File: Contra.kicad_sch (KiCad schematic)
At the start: 102 parts, among them J1 Conn_01x04, J2 Conn_01x02, SW1 SW_PUSH, SW2 SW_SPDT, U1 ProMicro

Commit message: add in NC symbols
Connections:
- no-connect marks 0 -> 6
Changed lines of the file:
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@@
 		(color 0 0 0 0)
 	)
+	(no_connect
+		(at 120.65 161.29)
+	)
+	(no_connect
+		(at 95.25 187.96)
+	)
+	(no_connect
+		(at 80.01 153.67)
+	)
+	(no_connect
+		(at 97.79 187.96)
+	)
+	(no_connect
+		(at 100.33 187.96)
+	)
+	(no_connect
+		(at 80.01 156.21)
+	)
 	(wire
 		(pts
@@
 	(wire
 		(pts
+			(xy 80.01 153.67) (xy 81.28 153.67)
+		)
+		(stroke
+			(width 0)
+			(type default)
+		)
+	)
+	(wire
+		(pts
 			(xy 176.53 96.52) (xy 195.58 96.52)
 		)
@@
 	(wire
 		(pts
+			(xy 119.38 161.29) (xy 120.65 161.29)
+		)
+		(stroke
+			(width 0)
+			(type default)
+		)
+	)
+	(wire
+		(pts
 			(xy 138.43 77.47) (xy 157.48 77.47)
 		)
@@
 	(wire
 		(pts
+			(xy 100.33 186.69) (xy 100.33 187.96)
+		)
+		(stroke
+			(width 0)
+			(type default)
+		)
+	)
+	(wire
+		(pts
 			(xy 81.28 115.57) (xy 100.33 115.57)
 		)
@@
 	(wire
 		(pts
+			(xy 80.01 156.21) (xy 81.28 156.21)
+		)
+		(stroke
+			(width 0)
+			(type default)
+		)
+	)
+	(wire
+		(pts
 			(xy 214.63 106.68) (xy 214.63 110.49)
 		)
@@
 	(wire
 		(pts
+			(xy 97.79 186.69) (xy 97.79 187.96)
+		)
+		(stroke
+			(width 0)
+			(type default)
+		)
+	)
+	(wire
+		(pts
 			(xy 195.58 87.63) (xy 195.58 91.44)
 		)
@@
 		)
 		(stroke
+			(width 0)
+			(type default)
+		)
+	)
+	(wire
+		(pts
+			(xy 95.25 186.69) (xy 95.25 187.96)
+		)
+		(stroke

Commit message: connect rows and colls
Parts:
- J1: footprint Connector_PinHeader_2.54mm:PinHeader_1x04_P2.54mm_Vertical -> Connector_PinHeader_2.54mm:PinHeader_1x04_P2.54mm_Horizontal
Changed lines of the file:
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@@
 			)
 		)
-		(property "Footprint" "Connector_PinHeader_2.54mm:PinHeader_1x04_P2.54mm_Vertical"
+		(property "Footprint" "Connector_PinHeader_2.54mm:PinHeader_1x04_P2.54mm_Horizontal"
 			(at 45.72 152.4 0)
 			(hide yes)

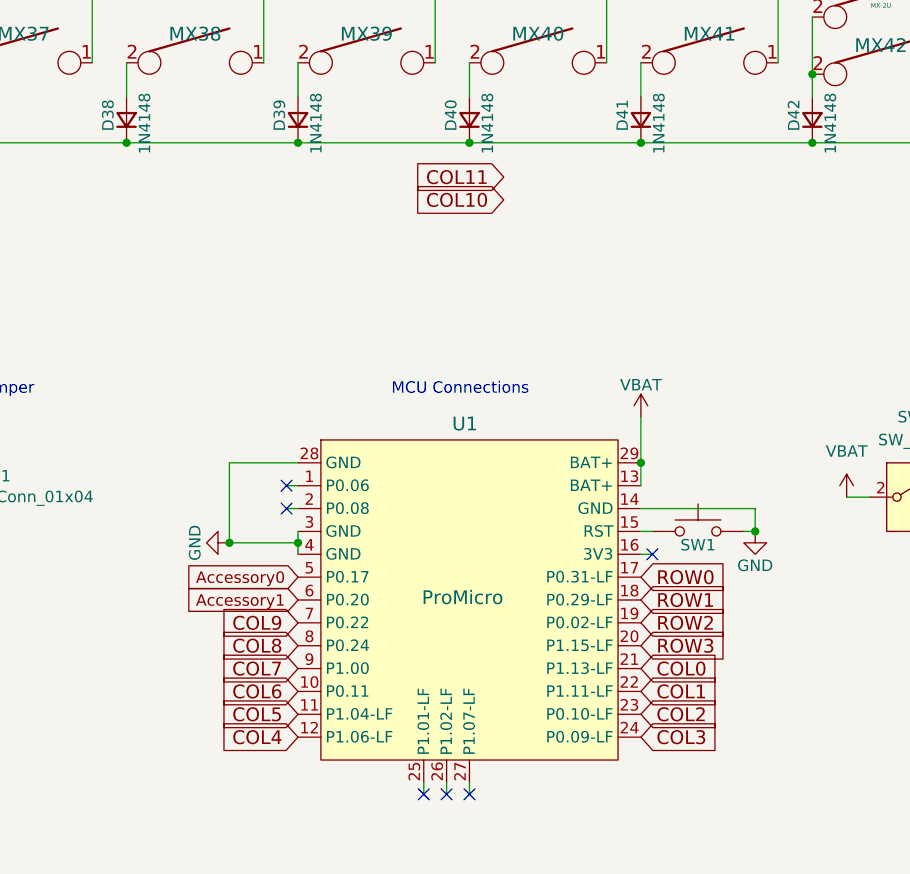
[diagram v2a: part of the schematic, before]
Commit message: update pinout of nice!nano
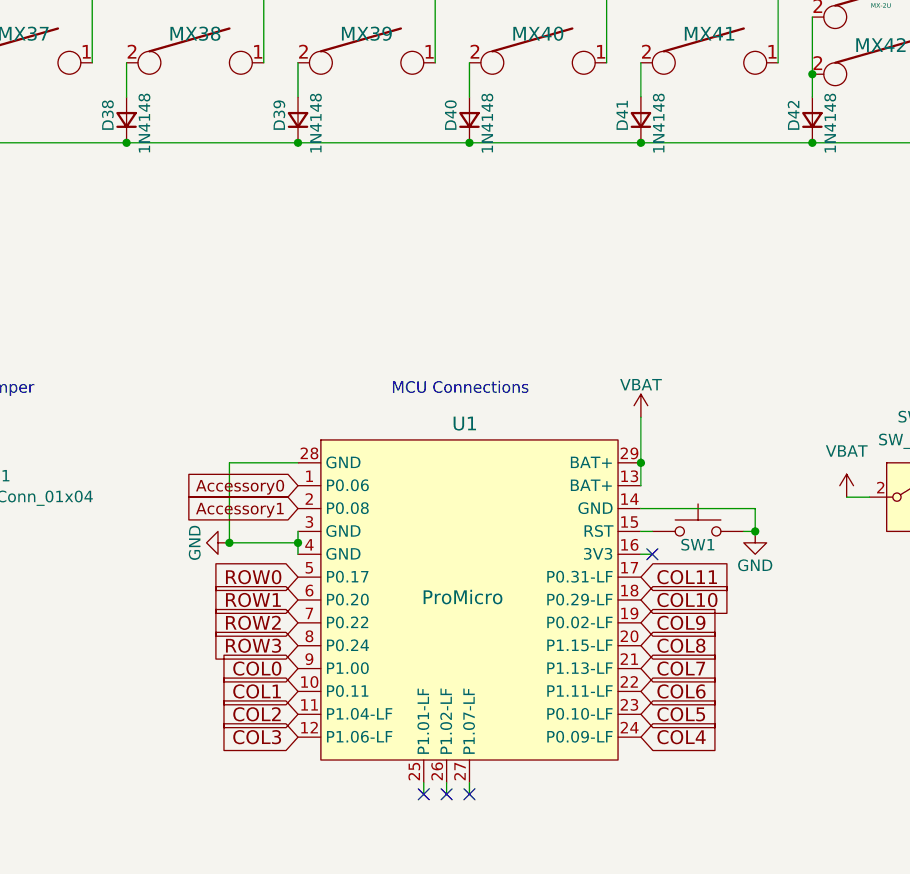
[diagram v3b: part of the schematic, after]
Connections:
- net Accessory0: now also U1.1 (P0.06); no longer U1.5 (P0.17)
- net Accessory1: now also U1.2 (P0.08); no longer U1.6 (P0.20)
- net COL0: now also U1.9 (P1.00); no longer U1.21 (P1.13-LF)
- net COL1: now also U1.10 (P0.11); no longer U1.22 (P1.11-LF)
- net COL10: now also U1.18 (P0.29-LF)
- net COL11: now also U1.17 (P0.31-LF)
- net COL2: now also U1.11 (P1.04-LF); no longer U1.23 (P0.10-LF)
- net COL3: now also U1.12 (P1.06-LF); no longer U1.24 (P0.09-LF)
- net COL4: now also U1.24 (P0.09-LF); no longer U1.12 (P1.06-LF)
- net COL5: now also U1.23 (P0.10-LF); no longer U1.11 (P1.04-LF)
- net COL6: now also U1.22 (P1.11-LF); no longer U1.10 (P0.11)
- net COL7: now also U1.21 (P1.13-LF); no longer U1.9 (P1.00)
- net COL8: now also U1.20 (P1.15-LF); no longer U1.8 (P0.24)
- net COL9: now also U1.19 (P0.02-LF); no longer U1.7 (P0.22)
- net ROW0: now also U1.5 (P0.17); no longer U1.17 (P0.31-LF)
- net ROW1: now also U1.6 (P0.20); no longer U1.18 (P0.29-LF)
- net ROW2: now also U1.7 (P0.22); no longer U1.19 (P0.02-LF)
- net ROW3: now also U1.8 (P0.24); no longer U1.20 (P1.15-LF)
- no-connect marks 6 -> 4

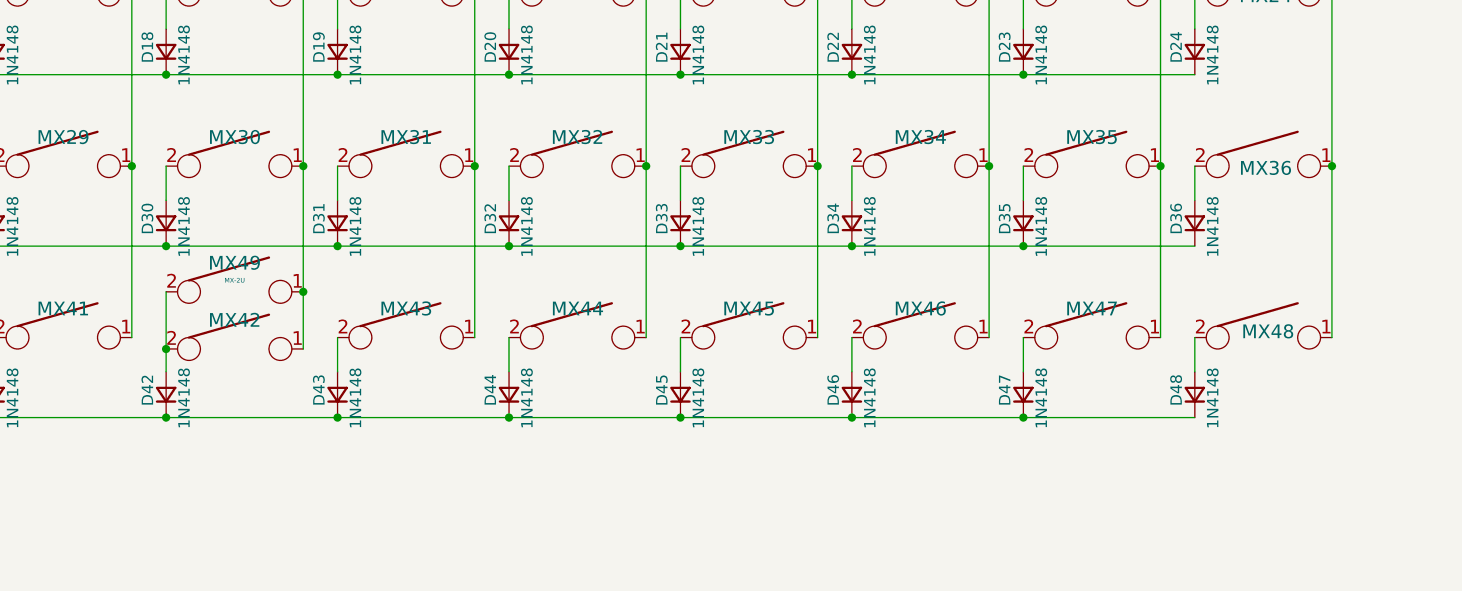
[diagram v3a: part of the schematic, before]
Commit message: remove 2 1U keys for a single 2U key for space
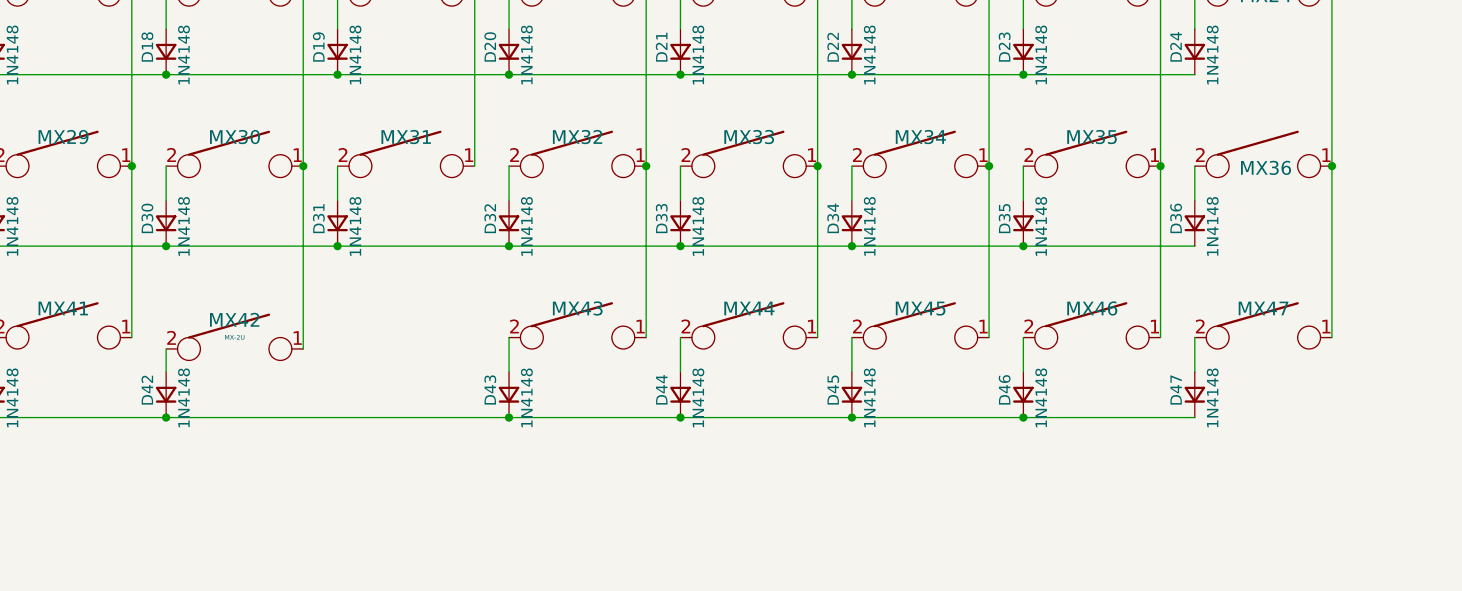
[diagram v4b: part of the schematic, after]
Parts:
- removed D48: 1N4148, Diode_THT:D_DO-35_SOD27_P7.62mm_Horizontal, symbol Device:D_Small
- removed MX48: MX-1U, MX_Hotswap:MX-Hotswap-1U, symbol keyboard_parts:KEYSW
- removed MX49: MX-2U, MX_Hotswap:MX-Hotswap-2U-ReversedStabilizers, symbol keyboard_parts:KEYSW
- MX42: value MX-1U -> MX-2U; footprint MX_Hotswap:MX-Hotswap-1U -> MX_Hotswap:MX-Hotswap-2U-ReversedStabilizers
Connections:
- net COL10: now also MX46.1; no longer MX47.1
- net COL11: now also MX47.1
- net COL6: no longer MX43.1
- net COL7: now also MX43.1; no longer MX44.1
- net COL8: now also MX44.1; no longer MX45.1
- net COL9: now also MX45.1; no longer MX46.1
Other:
- moved on the sheet: D43, D44, D45, D46, D47, MX43, MX44, MX45, MX46, MX47

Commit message: make PCB 4 layers
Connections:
- net VBAT: now also SW2.3 (C); no longer SW2.2 (B)
- net at J2.1 (Pin_1): now also SW2.2 (B); no longer SW2.3 (C)
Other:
- moved on the sheet: SW2
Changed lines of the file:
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@@
 	)
 	(junction
-		(at 157.48 160.02)
+		(at 157.48 165.1)
 		(diameter 0)
 		(color 0 0 0 0)
@@
 	(wire
 		(pts
-			(xy 157.48 152.4) (xy 157.48 160.02)
-		)
-		(stroke
-			(width 0)
-			(type default)
-		)
-	)
-	(wire
-		(pts
 			(xy 138.43 58.42) (xy 157.48 58.42)
 		)
@@
 	(wire
 		(pts
-			(xy 134.62 68.58) (xy 134.62 87.63)
+			(xy 144.78 165.1) (xy 157.48 165.1)
 		)
 		(stroke
@@
 	(wire
 		(pts
-			(xy 36.83 58.42) (xy 43.18 58.42)
+			(xy 134.62 68.58) (xy 134.62 87.63)
 		)
 		(stroke
@@
 	(wire
 		(pts
-			(xy 154.94 152.4) (xy 157.48 152.4)
+			(xy 36.83 58.42) (xy 43.18 58.42)
 		)
 		(stroke
@@
 	(wire
 		(pts
+			(xy 157.48 165.1) (xy 157.48 160.02)
+		)
+		(stroke
+			(width 0)
+			(type default)
+		)
+	)
+	(wire
+		(pts
 			(xy 248.92 38.1) (xy 248.92 49.53)
 		)
@@
 	(wire
 		(pts
-			(xy 154.94 157.48) (xy 158.75 157.48)
-		)
-		(stroke
-			(width 0)
-			(type default)
-		)
-	)
-	(wire
-		(pts
 			(xy 210.82 68.58) (xy 210.82 87.63)
 		)
@@
 	(wire
 		(pts
+			(xy 144.78 160.02) (xy 144.78 165.1)
+		)
+		(stroke
+			(width 0)
+			(type default)
+		)
+	)
+	(wire
+		(pts
 			(xy 100.33 77.47) (xy 119.38 77.47)
 		)
@@
 	(wire
 		(pts
+			(xy 154.94 157.48) (xy 158.75 157.48)
+		)
+		(stroke
+			(width 0)
+			(type default)
+		)
+	)
+	(wire
+		(pts
 			(xy 115.57 87.63) (xy 115.57 106.68)
 		)
@@
 	(symbol
 		(lib_id "Switch:SW_SPDT")
-		(at 149.86 154.94 0)
+		(at 149.86 157.48 180)
 		(unit 1)
 		(body_style 1)
@@
 		(fields_autoplaced yes)
 		(property "Reference" "SW2"
-			(at 149.86 146.05 0)
+			(at 149.86 148.59 0)
 			(show_name no)
 			(do_not_autoplace no)
@@
 		)
 		(property "Value" "SW_SPDT"
-			(at 149.86 148.59 0)
+			(at 149.86 151.13 0)
 			(show_name no)
 			(do_not_autoplace no)
@@
 		)
 		(property "Footprint" "Button_Switch_THT:SW_Slide_SPDT_Angled_CK_OS102011MA1Q"
-			(at 149.86 154.94 0)
+			(at 149.86 157.48 0)
 			(hide yes)
 			(show_name no)
@@
 		)
 		(property "Datasheet" ""
-			(at 149.86 162.56 0)
+			(at 149.86 149.86 0)
 			(hide yes)
 			(show_name no)
@@
 		)
 		(property "Description" "Switch, single pole double throw"
-			(at 149.86 154.94 0)
+			(at 149.86 157.48 0)
 			(hide yes)
 			(show_name no)
@@
 	(symbol
 		(lib_id "power:GND")
-		(at 157.48 160.02 0)
+		(at 157.48 165.1 0)
 		(unit 1)
 		(body_style 1)
@@
 		(fields_autoplaced yes)
 		(property "Reference" "#PWR01"
-			(at 157.48 166.37 0)
+			(at 157.48 171.45 0)
 			(hide yes)
 			(show_name no)
@@
 		)
 		(property "Value" "GND"
-			(at 157.48 165.1 0)
+			(at 157.48 170.18 0)
 			(show_name no)
 			(do_not_autoplace no)
@@
 		)
 		(property "Footprint" ""
-			(at 157.48 160.02 0)
+			(at 157.48 165.1 0)
 			(hide yes)
 			(show_name no)
@@
 		)
 		(property "Datasheet" ""
-			(at 157.48 160.02 0)
+			(at 157.48 165.1 0)
 			(hide yes)
 			(show_name no)
@@
 		)
 		(property "Description" "Power symbol creates a global label with name \"GND\" , ground"
-			(at 157.48 160.02 0)
+			(at 157.48 165.1 0)
 			(hide yes)
 			(show_name no)

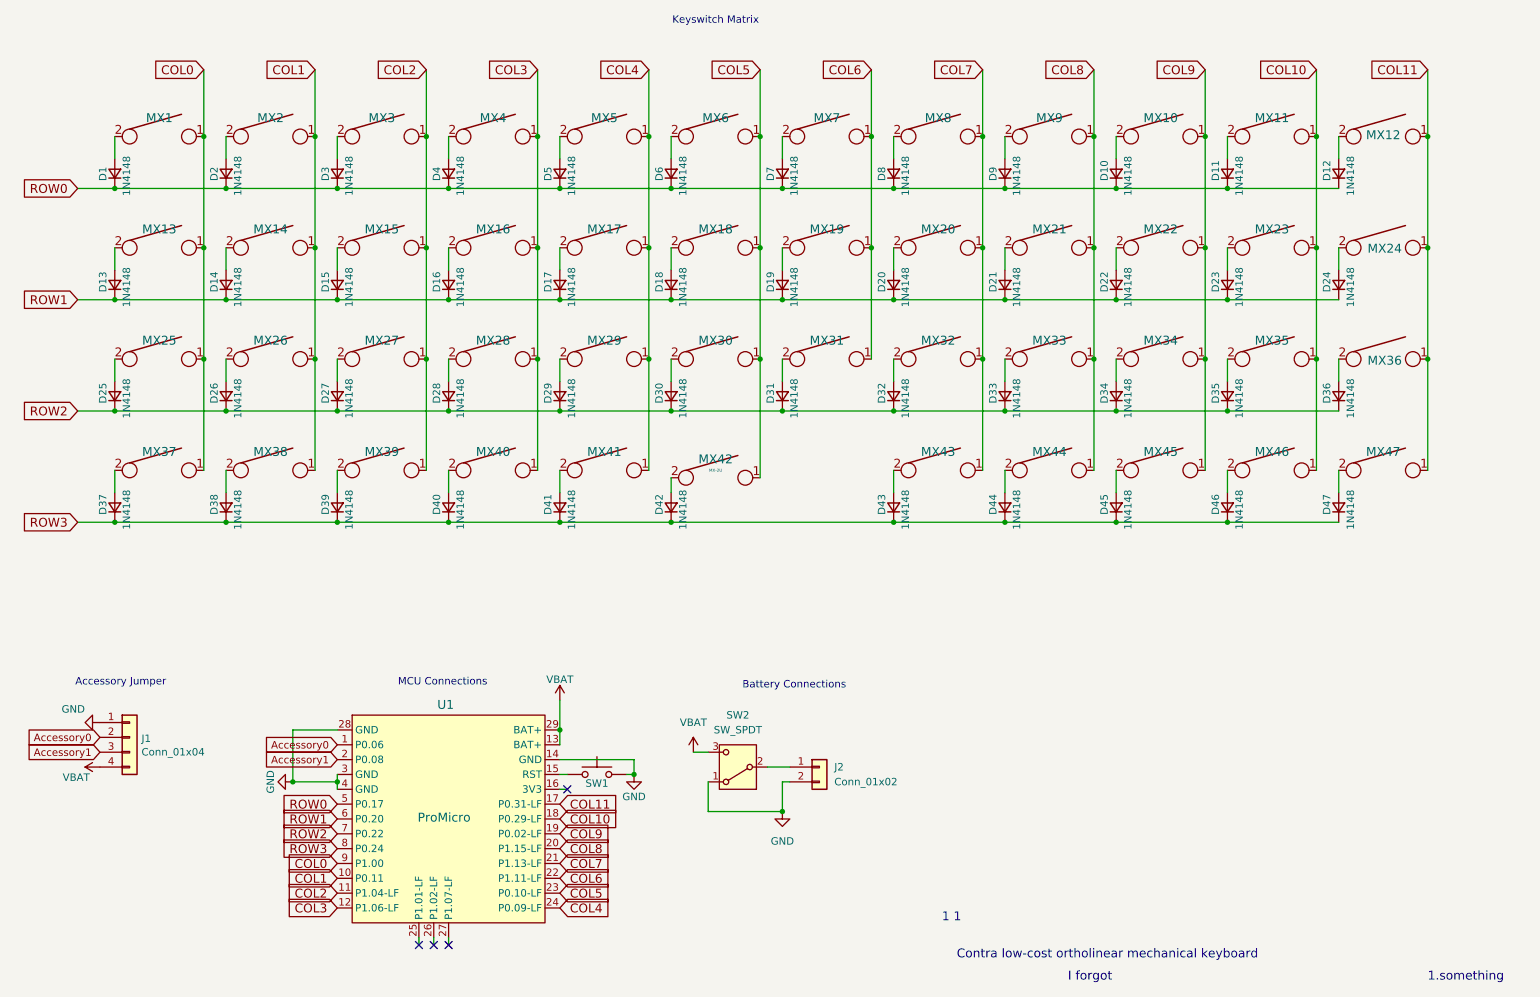
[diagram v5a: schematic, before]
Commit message: start adding in Neopixels
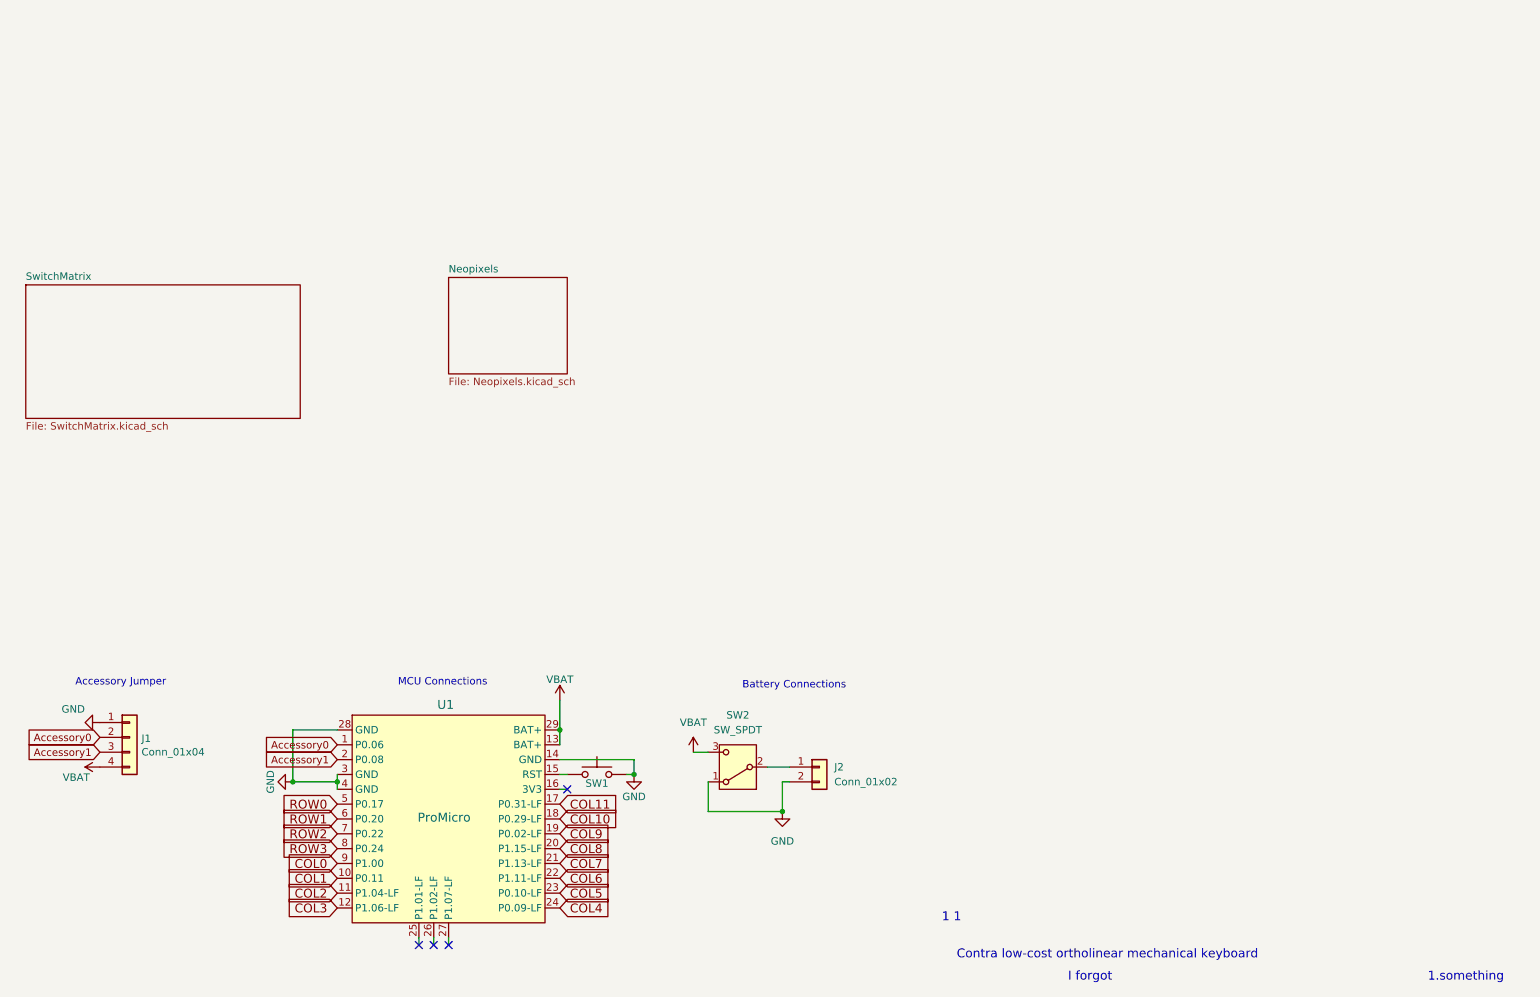
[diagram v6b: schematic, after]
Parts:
- removed D1, D10, D11, D12, D13, D14, D15, D16, D17, D18, D19, D2, D20, D21, D22, D23, D24, D25, D26, D27, D28, D29, D3, D30, D31, D32, D33, D34, D35, D36, D37, D38, D39, D4, D40, D41, D42, D43, D44, D45, D46, D47, D5, D6, D7, D8, D9: 1N4148, Diode_THT:D_DO-35_SOD27_P7.62mm_Horizontal, symbol Device:D_Small
- removed MX1, MX10, MX11, MX12, MX13, MX14, MX15, MX16, MX17, MX18, MX19, MX2, MX20, MX21, MX22, MX23, MX24, MX25, MX26, MX27, MX28, MX29, MX3, MX30, MX31, MX32, MX33, MX34, MX35, MX36, MX37, MX38, MX39, MX4, MX40, MX41, MX43, MX44, MX45, MX46, MX47, MX5, MX6, MX7, MX8, MX9: MX-1U, MX_Hotswap:MX-Hotswap-1U, symbol keyboard_parts:KEYSW
- removed MX42: MX-2U, MX_Hotswap:MX-Hotswap-2U-ReversedStabilizers, symbol keyboard_parts:KEYSW
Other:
- added sheet Neopixels (Neopixels.kicad_sch)
- added sheet SwitchMatrix (SwitchMatrix.kicad_sch)
- note removed: "Keyswitch Matrix"

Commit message: get the Corne reference set up
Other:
- added sheet CorneReference (CorneReference.kicad_sch)
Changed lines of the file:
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@@
+	)
+	(sheet
+		(at 214.63 60.96)
+		(size 53.34 27.94)
+		(exclude_from_sim no)
+		(in_bom yes)
+		(on_board yes)
+		(dnp no)
+		(fields_autoplaced yes)
+		(stroke
+			(width 0.1524)
+			(type solid)
+		)
+		(fill
+			(color 0 0 0 0)
+		)
+		(property "Sheetname" "CorneReference"
+			(at 214.63 60.2484 0)
+			(show_name no)
+			(do_not_autoplace no)
+			(effects
+				(font
+					(size 1.27 1.27)
+				)
+				(justify left bottom)
+			)
+		)
+		(property "Sheetfile" "CorneReference.kicad_sch"
+			(at 214.63 89.4846 0)
+			(show_name no)
+			(do_not_autoplace no)
+			(effects
+				(font
+					(size 1.27 1.27)
+				)
+				(justify left top)
+			)
+		)
+		(instances
+			(project "Contra"
+				(path "/490ed6d6-ce6d-4821-aa52-98b9130151cb"
+					(page "4")
+				)
+			)
+		)
 	)
 	(sheet
